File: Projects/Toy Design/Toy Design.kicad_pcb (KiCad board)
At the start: 2 copper layers, 100 x 100 mm, 82 parts, among them J1 Conn_01x01_Pin, J2 Conn_01x01_Pin, U1 TLV61048DBVR, U10 STM32G030K6T6, U11 MCP3208-CI/SL, U12 74HC595, U13 74HC595, U14 74HC595, U15 74HC595, U16 74HC595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

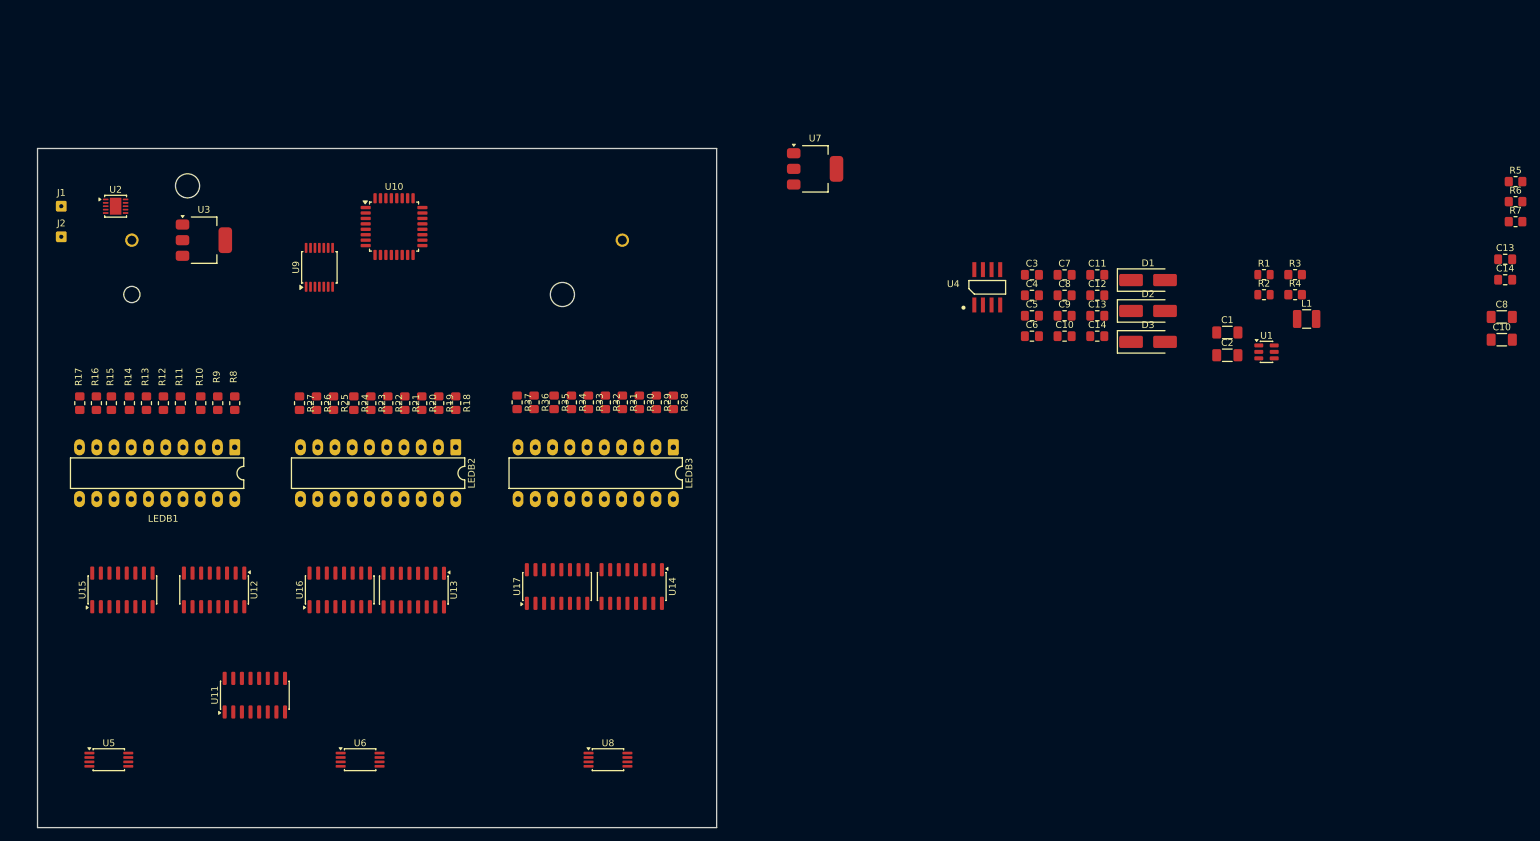
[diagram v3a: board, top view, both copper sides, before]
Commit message: Began routing up to te serial in parallel out ICs
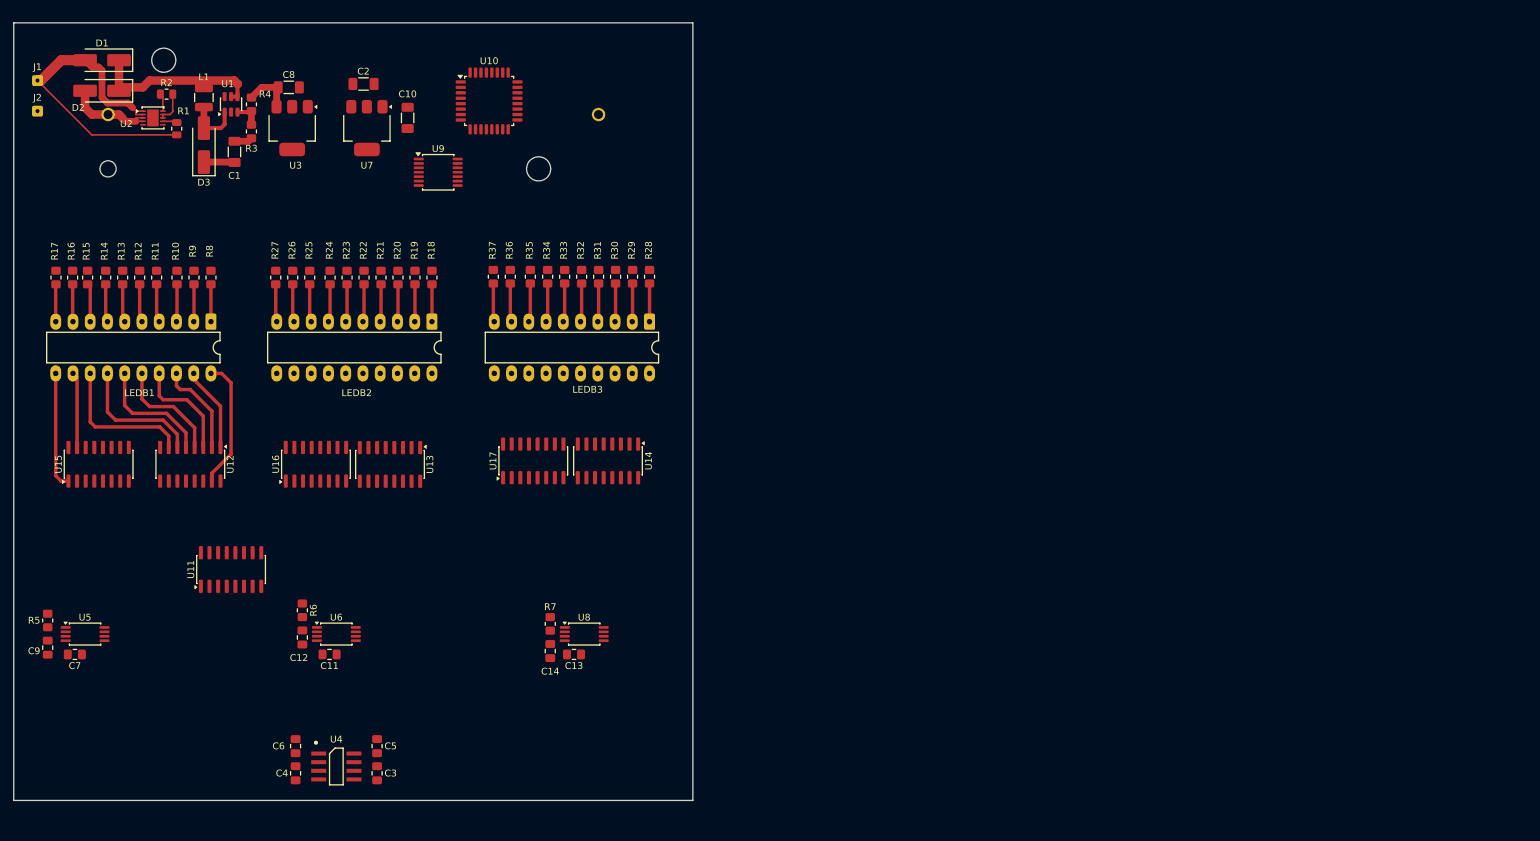
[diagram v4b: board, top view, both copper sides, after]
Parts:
- removed the C10 at (251.2, 77.6)
- removed the C13 at (256.0, 74.6)
- removed the C13 at (316.1, 66.3)
- removed the C14 at (316.1, 69.3)
- removed the C14 at (256.0, 77.6)
- removed the C8 at (251.2, 71.6)
- added C13: 100nF, Capacitor_SMD:C_0805_2012Metric_Pad1.18x1.45mm_HandSolder, F.Cu at (179.0, 124.5)
- added C14: 100nF, Capacitor_SMD:C_0805_2012Metric_Pad1.18x1.45mm_HandSolder, F.Cu at (175.5, 124.0)
- moved R5 225.6 mm to (101.5, 119.5), turned to -90 degrees
- moved R6 188.5 mm to (139.0, 118.0), turned to -90 degrees
- moved C8 181.8 mm to (137.0, 41.0)
- moved L1 165.6 mm to (124.5, 42.5), turned to -90 degrees
- moved C10 164.4 mm to (154.5, 45.5), turned to 90 degrees
- moved R2 164.3 mm to (119.0, 42.0)
- moved R1 161.5 mm to (120.5, 47.1), turned to 90 degrees
- moved C9 157.5 mm to (101.5, 123.5), turned to -90 degrees
- moved D2 157.4 mm to (109.5, 41.5), turned to 180 degrees
- moved D1 157.4 mm to (109.5, 37.0), turned to 180 degrees
- moved U1 156.8 mm to (128.5, 43.5), turned to 90 degrees
- moved R4 156.2 mm to (131.5, 43.5), turned to -90 degrees
- moved C7 156.1 mm to (105.5, 124.5), turned to 180 degrees
- moved R3 155.1 mm to (131.5, 47.5), turned to -90 degrees
- moved R7 154.0 mm to (175.5, 120.0), turned to -90 degrees
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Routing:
- net Net-(D1-A): track 0.00 -> 47.6 mm
- net Net-(D1-K): track 0.00 -> 26.2 mm
- net Net-(U12-QH): track 0.00 -> 21.3 mm
- net Net-(U12-QG): track 0.00 -> 19.3 mm
- net Net-(U12-QA): track 0.00 -> 19.2 mm
- net Net-(U12-QF): track 0.00 -> 17.6 mm
- net Net-(U15-QB): track 0.00 -> 17.3 mm
- net Net-(U12-QE): track 0.00 -> 16.2 mm
- net Net-(U12-QD): track 0.00 -> 15.6 mm
- net Net-(U12-QC): track 0.00 -> 13.9 mm
- net Net-(D2-A): track 0.00 -> 13.4 mm
- net Net-(U12-QB): track 0.00 -> 12.5 mm
- net +5.6V: track 0.00 -> 12.0 mm
- net Net-(U15-QA): track 0.00 -> 11.2 mm
- net Net-(D3-A): track 0.00 -> 8.19 mm
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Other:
- board size 100 x 100 mm -> 100 x 114.5 mm

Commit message: Finshed most signal routing
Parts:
- moved U11 33.8 mm to (162.2, 110.5)
- moved C4 32.9 mm to (152.5, 112.5)
- moved C3 30.8 mm to (141.2, 112.5)
- moved C5 29.6 mm to (152.5, 108.5)
- moved U4 29.6 mm to (146.5, 111.5)
- moved C6 28.8 mm to (140.2, 109.2), turned to 180 degrees
- moved C11 14.0 mm to (147.5, 137.8)
- moved C12 14.0 mm to (143.5, 135.2)
- moved C13 14.0 mm to (183.5, 137.8)
- moved C7 14.0 mm to (110.0, 137.8)
- moved R6 14.0 mm to (143.5, 131.2)
- moved U5 14.0 mm to (111.5, 134.8)
- moved U6 14.0 mm to (148.5, 134.8)
- moved U8 14.0 mm to (185.0, 134.8)
- moved R5 13.1 mm to (106.0, 131.8)
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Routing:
- net RCLK_LED: track 0.00 -> 89.6 mm
- net MISO_SPI1: track 0.00 -> 71.2 mm
- net OUT_U5: track 0.00 -> 68.5 mm
- net Net-(U11-CLK): track 0.00 -> 59.1 mm
- net Net-(U11-Din): track 0.00 -> 57.5 mm
- net Net-(U11-~{CS}/SHDN): track 0.00 -> 56.9 mm
- net SPI2_SCK_LED: track 0.00 -> 37.6 mm
- net OUT_U8: track 0.00 -> 37.0 mm
- net OUT_U6: track 0.00 -> 34.5 mm
- net SPI2_MOSI_LED: track 0.00 -> 34.3 mm
- net ~{SRCLR}: track 0.00 -> 31.0 mm
- net OUT2_U4: track 0.00 -> 25.0 mm
- net +5V: track 0.00 -> 20.8 mm
- net Net-(U13-QH): track 0.00 -> 17.9 mm
- net Net-(U14-QH): track 0.00 -> 17.7 mm
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
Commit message: 90% Routing complete
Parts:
- moved C10 3.09 mm to (153.8, 48.5)
- moved R5 2.57 mm to (108.2, 130.5), turned to 90 degrees
- moved R6 1.25 mm to (144.8, 131.2), turned to 180 degrees
- turned U15 to -90 degrees
- turned U16 to -90 degrees
- turned U17 to -90 degrees
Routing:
- net +5V: track 20.8 -> 367.1 mm, vias 0 -> 4
- net ~{SRCLR}: track 31.0 -> 198.8 mm, vias 0 -> 7
- net SPI2_SCK_LED: track 37.6 -> 203.3 mm, vias 0 -> 8
- net RCLK_LED: track 89.6 -> 183.3 mm, vias 0 -> 5
- net SPI2_MOSI_LED: track 34.3 -> 93.4 mm, vias 0 -> 2
- net +3.3V: track 0.00 -> 51.1 mm, vias 0 -> 2
- net Net-(U15-QA): track 11.2 -> 28.3 mm
- net Net-(U16-QA): track 10.9 -> 25.0 mm
- net Net-(U17-QA): track 10.4 -> 24.3 mm
- net GND: track 9.62 -> 17.8 mm, vias 0 -> 130
- net Net-(U16-QB): track 17.2 -> 25.2 mm
- net Net-(U15-QB): track 17.3 -> 25.2 mm
- net Net-(U17-QB): track 16.5 -> 24.2 mm
- net OUT_U6: track 34.5 -> 36.2 mm
- net OUT_U5: track 68.5 -> 70.2 mm
- added copper zone on F.Cu, net +3.3V
- added copper zone on F.Cu, net +5V
- added copper zone on B.Cu, net GND
- added copper zone on F.Cu, net GND

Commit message: updated sonme stuff
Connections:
- U9 pad 7: unconnected-(U9-GND-Pad7) -> GND
- U9 pad 8: unconnected-(U9-OE-Pad8) -> +5V
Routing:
- net +5.6V: track 12.0 -> 24.8 mm
- net GND: vias 130 -> 176

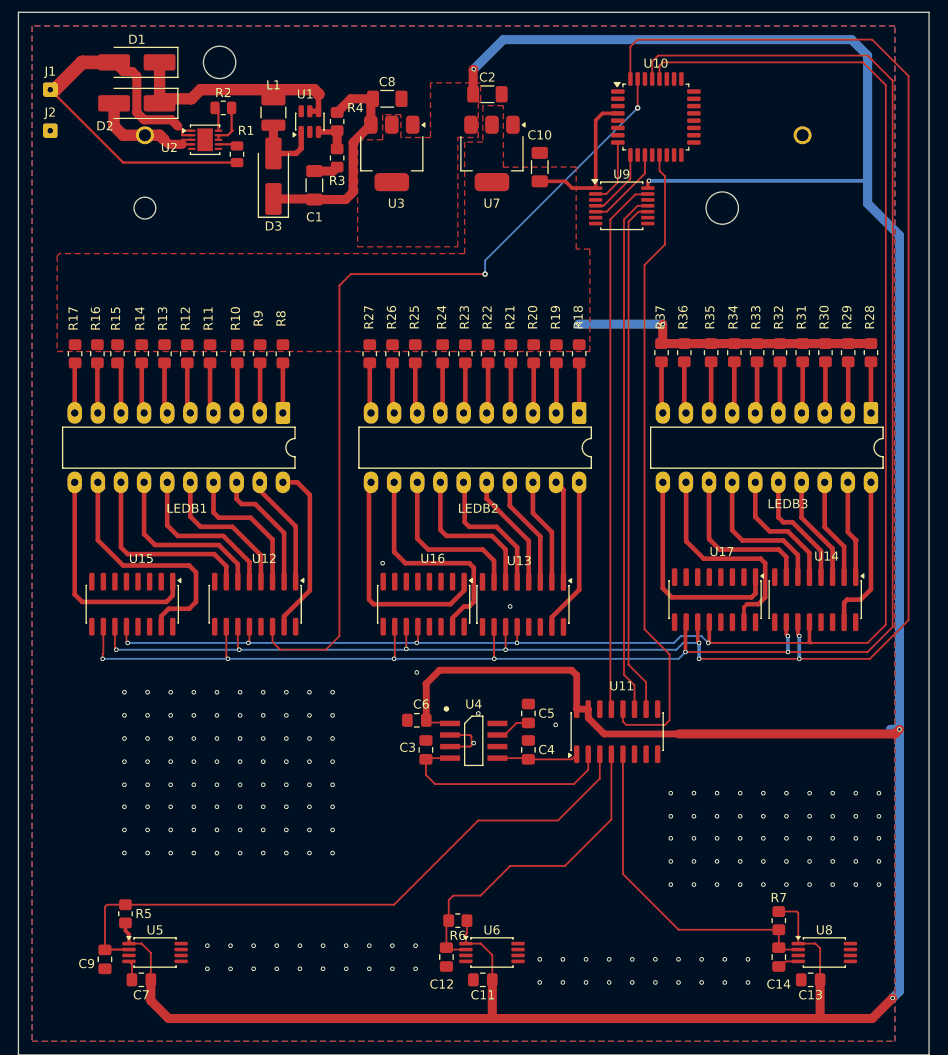
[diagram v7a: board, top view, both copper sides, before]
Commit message: Updating with programmer nets but no connector YET
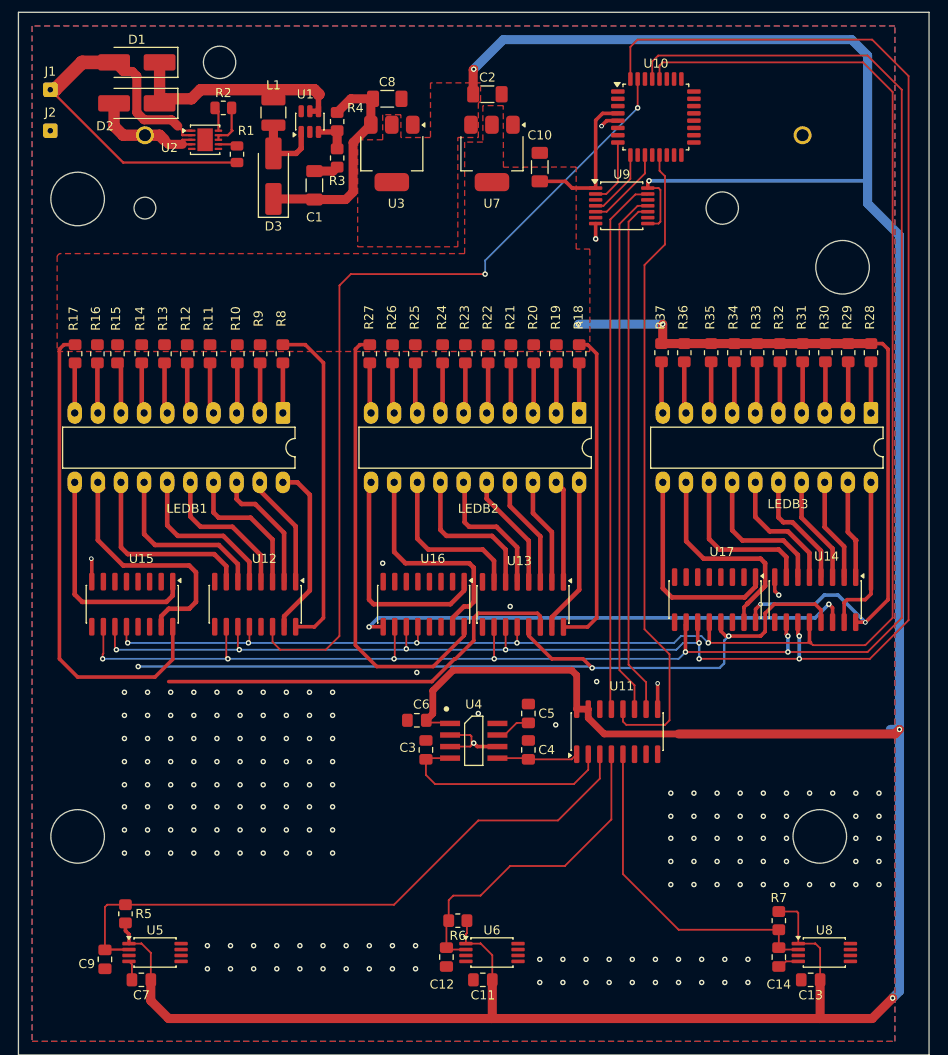
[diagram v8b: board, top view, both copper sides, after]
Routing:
- net +3.3V: track 51.1 -> 276.0 mm, vias 2 -> 4
- net ~{OE}: track 0.00 -> 93.6 mm, vias 0 -> 3
- net Net-(U14-SER): track 0.00 -> 55.2 mm, vias 0 -> 2
- net Net-(U13-SER): track 0.00 -> 46.7 mm
- net GND: track 17.8 -> 32.1 mm
- net +5V: track 367.1 -> 372.7 mm
- net ~{SRCLR}: track 198.8 -> 199.6 mm
- net RCLK_LED: track 183.3 -> 184.2 mm
- net Net-(U17-QA): track 24.3 -> 23.6 mm
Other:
- outline, holes or cut-outs redrawn
